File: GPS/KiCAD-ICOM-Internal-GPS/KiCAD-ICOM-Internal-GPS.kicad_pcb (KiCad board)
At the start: 2 copper layers, 2 parts, among them J1 AXK640347YG, U1 MAX-M10M-00B

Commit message: updated schematic & PCB
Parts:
- J1: value AXK640347YG -> ICOM-J1; footprint AXK640347YG:AXK640347YG -> ICOM-J1:ICOM-J1
- moved J1 1.77 mm to (118.3, 59.9)
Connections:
- J1 pad 14: unconnected-(J1-Pad14) -> Net-(J1-RX/OPT1)
- J1 pad 15: unconnected-(J1-Pad15) -> Net-(J1-TX/OPT2)
- J1 pad 17: unconnected-(J1-Pad17) -> Net-(J1-GND-Pad17)
- U1 pad 1: unconnected-(U1-GND-Pad1) -> Net-(J1-GND-Pad17)
- U1 pad 2: unconnected-(U1-TXD-Pad2) -> Net-(J1-RX/OPT1)
- U1 pad 3: unconnected-(U1-RXD-Pad3) -> Net-(J1-TX/OPT2)
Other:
- board outline added: 20 x 35 mm

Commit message: updated schematic a bit
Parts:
- J1: footprint ICOM-J1:ICOM-J1 -> AXK640347YG:AXK640347YG
- moved J1 39.2 mm to (149.4, 83.8)
- moved U1 39.2 mm to (150.3, 96.3)
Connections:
- net Net-(J1-RX/OPT1) renamed GPS-TX
- net Net-(J1-TX/OPT2) renamed GPS-RX
- J1 pad 17: Net-(J1-GND-Pad17) -> GND
- J1 pad 2: unconnected-(J1-GND-Pad2) -> GND
- J1 pad 38: unconnected-(J1-+5V-Pad38) -> +5V
- J1 pad 39: unconnected-(J1-GND-Pad39) -> GND
- U1 pad 1: Net-(J1-GND-Pad17) -> GND
- U1 pad 10: unconnected-(U1-GND-Pad10) -> GND
- U1 pad 11: unconnected-(U1-RF_IN-Pad11) -> ANT-RF
- U1 pad 12: unconnected-(U1-GND-Pad12) -> GND
- U1 pad 13: unconnected-(U1-LNA_EN-Pad13) -> ANT-PWR-ON
- U1 pad 16: unconnected-(U1-SDA-Pad16) -> SDA
- U1 pad 17: unconnected-(U1-SCL-Pad17) -> SCL
- U1 pad 4: unconnected-(U1-TIMEPULSE-Pad4) -> PPS
- U1 pad 5: unconnected-(U1-EXTINT-Pad5) -> EXTINT
- U1 pad 6: unconnected-(U1-V_BCKP-Pad6) -> V-BACKUP
- U1 pad 7: unconnected-(U1-V_IO-Pad7) -> +3.3V
- U1 pad 8: unconnected-(U1-VCC-Pad8) -> +3.3V
- U1 pad 9: unconnected-(U1-RESET_N-Pad9) -> RESET

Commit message: updated v1.0 design
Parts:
- added B1: MS518SE, MS518SE:MS518SE-FL35E, F.Cu at (154.2, 93.2)
- added J2: U.FL-R-SMT-1_10_, U.FL-R-SMT-1_10:HRS_U.FL-R-SMT-1_10_, F.Cu at (143.8, 111.6)
- J1: footprint AXK640347YG:AXK640347YG -> ICOM-J1-J2:ICOM-J1-J2
- moved U1 6.66 mm to (147.1, 102.1), turned to -90 degrees
- moved J1 0.33 mm to (149.3, 83.5)
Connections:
- U1 pad 13: ANT-PWR-ON -> unconnected-(U1-LNA_EN-Pad13)

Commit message: minor save
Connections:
- U1 pad 5: EXTINT -> unconnected-(U1-EXTINT-Pad5)
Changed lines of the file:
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@@
 	(net 44 "V-BACKUP")
 	(net 45 "SCL")
-	(net 46 "EXTINT")
-	(net 47 "SDA")
-	(net 48 "+3.3V")
-	(net 49 "ANT-RF")
-	(net 50 "unconnected-(U1-LNA_EN-Pad13)")
+	(net 46 "SDA")
+	(net 47 "+3.3V")
+	(net 48 "ANT-RF")
+	(net 49 "unconnected-(U1-LNA_EN-Pad13)")
+	(net 50 "unconnected-(U1-EXTINT-Pad5)")
 	(footprint "ICOM-J1-J2:ICOM-J1-J2"
 		(layer "F.Cu")
@@
 		(tags "MAX-M10M-00B ")
 		(property "Reference" "U1"
-			(at 0 0 -90)
+			(at 0 0 0)
 			(unlocked yes)
 			(layer "F.SilkS")
@@
 			(unlocked yes)
 			(layer "F.Fab")
+			(hide yes)
 			(effects
 				(font
@@
 			(layer "F.Fab")
 		)
-		(fp_text user "${REFERENCE}"
-			(at 0 0 -90)
-			(unlocked yes)
-			(layer "F.Fab")
-			(effects
-				(font
-					(size 1 1)
-					(thickness 0.15)
-				)
-			)
-		)
 		(pad "1" smd rect
 			(at -4.4577 -4.399999 270)
@@
 			(size 1.397 0.8382)
 			(layers "F.Cu" "F.Paste" "F.Mask")
-			(net 46 "EXTINT")
+			(net 50 "unconnected-(U1-EXTINT-Pad5)")
 			(pinfunction "EXTINT")
-			(pintype "input")
+			(pintype "input+no_connect")
 		)
 		(pad "6" smd rect
@@
 			(size 1.397 0.8382)
 			(layers "F.Cu" "F.Paste" "F.Mask")
-			(net 48 "+3.3V")
+			(net 47 "+3.3V")
 			(pinfunction "V_IO")
 			(pintype "power_in")
@@
 			(size 1.397 0.8382)
 			(layers "F.Cu" "F.Paste" "F.Mask")
-			(net 48 "+3.3V")
+			(net 47 "+3.3V")
 			(pinfunction "VCC")
 			(pintype "power_in")
@@
 			(size 1.397 0.8382)
 			(layers "F.Cu" "F.Paste" "F.Mask")
-			(net 49 "ANT-RF")
+			(net 48 "ANT-RF")
 			(pinfunction "RF_IN")
 			(pintype "input")
@@
 			(size 1.397 0.8382)
 			(layers "F.Cu" "F.Paste" "F.Mask")
-			(net 50 "unconnected-(U1-LNA_EN-Pad13)")
+			(net 49 "unconnected-(U1-LNA_EN-Pad13)")
 			(pinfunction "LNA_EN")
 			(pintype "output+no_connect")
@@
 			(net 1 "unconnected-(U1-VCC_RF-Pad14)")
 			(pinfunction "VCC_RF")
-			(pintype "output")
+			(pintype "output+no_connect")
 		)
 		(pad "15" smd rect
@@
 			(net 2 "unconnected-(U1-VIO_SEL-Pad15)")
 			(pinfunction "VIO_SEL")
-			(pintype "input")
+			(pintype "input+no_connect")
 		)
 		(pad "16" smd rect
@@
 			(size 1.397 0.8382)
 			(layers "F.Cu" "F.Paste" "F.Mask")
-			(net 47 "SDA")
+			(net 46 "SDA")
 			(pinfunction "SDA")
 			(pintype "bidirectional")
@@
 			(net 3 "unconnected-(U1-SAFEBOOT_N-Pad18)")
 			(pinfunction "SAFEBOOT_N")
-			(pintype "input")
+			(pintype "input+no_connect")
 		)
 		(model "/Users/fredericdruppel/Documents/Documents Importants/Taff/MSF/MSF-Telecom-GitHub/ICOM-Internal-Modules/CAD-Libs/UBX-MAX-M10S/MOD18_MAX-M10M_UBL.step"
@@
 		(at 154.178 93.218 180)
 		(property "Reference" "B1"
-			(at 0 -3.4925 180)
+			(at 0 0 180)
 			(layer "F.SilkS")
 			(effects
@@
 			(at 0 0 180)
 			(layer "F.Fab")
+			(hide yes)
 			(effects
 				(font
@@
 		(at 143.764 111.627 180)
 		(property "Reference" "J2"
-			(at -0.060105 -2.311695 180)
+			(at 0 0 180)
 			(layer "F.SilkS")
 			(effects
@@
 			(at 7.5777 3.09926 180)
 			(layer "F.Fab")
+			(hide yes)
 			(effects
 				(font
@@
 			(size 1 1.05)
 			(layers "F.Cu" "F.Paste" "F.Mask")
-			(net 49 "ANT-RF")
+			(net 48 "ANT-RF")
 			(pintype "passive")
 			(solder_mask_margin 0.102)

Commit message: updated schematic and pcb
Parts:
- added C1: 10nF, Capacitor_SMD:C_0603_1608Metric, F.Cu at (144.5, 108.7)
- added C2: 10nF, Capacitor_SMD:C_0603_1608Metric, F.Cu at (143.5, 95.8)
- added C3: 10nF, Capacitor_SMD:C_0603_1608Metric, F.Cu at (146.8, 95.8)
- added C4: 10nF, Capacitor_SMD:C_0603_1608Metric, F.Cu at (140.0, 91.4)
- added J3: Conn_01x08, Connector_PinSocket_2.54mm:PinSocket_1x08_P2.54mm_Vertical, F.Cu at (156.2, 93.7)
- added L1: 27nH, Inductor_SMD:L_0402_1005Metric, F.Cu at (143.0, 111.5)
- added R1: 10, Resistor_SMD:R_0603_1608Metric, F.Cu at (144.5, 110.2)
- added U2: TC2015-3.3VxCTTR, Package_TO_SOT_SMD:SOT-23-5, F.Cu at (142.5, 91.4)
- moved J2 4.19 mm to (139.6, 111.5), turned to 90 degrees
- moved B1 3.28 mm to (150.9, 93.2)
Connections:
- J2 pad 2: ANT-RF -> Net-(J2-Pad2)

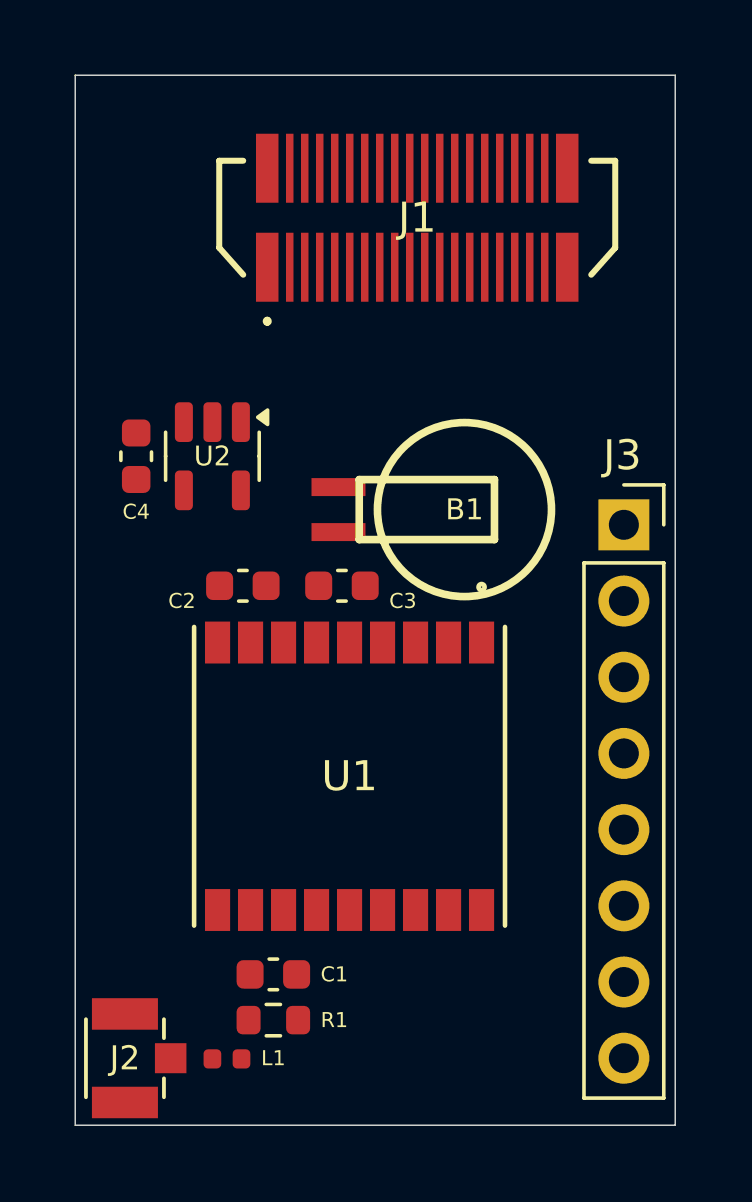
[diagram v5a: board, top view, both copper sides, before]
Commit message: Routed traces
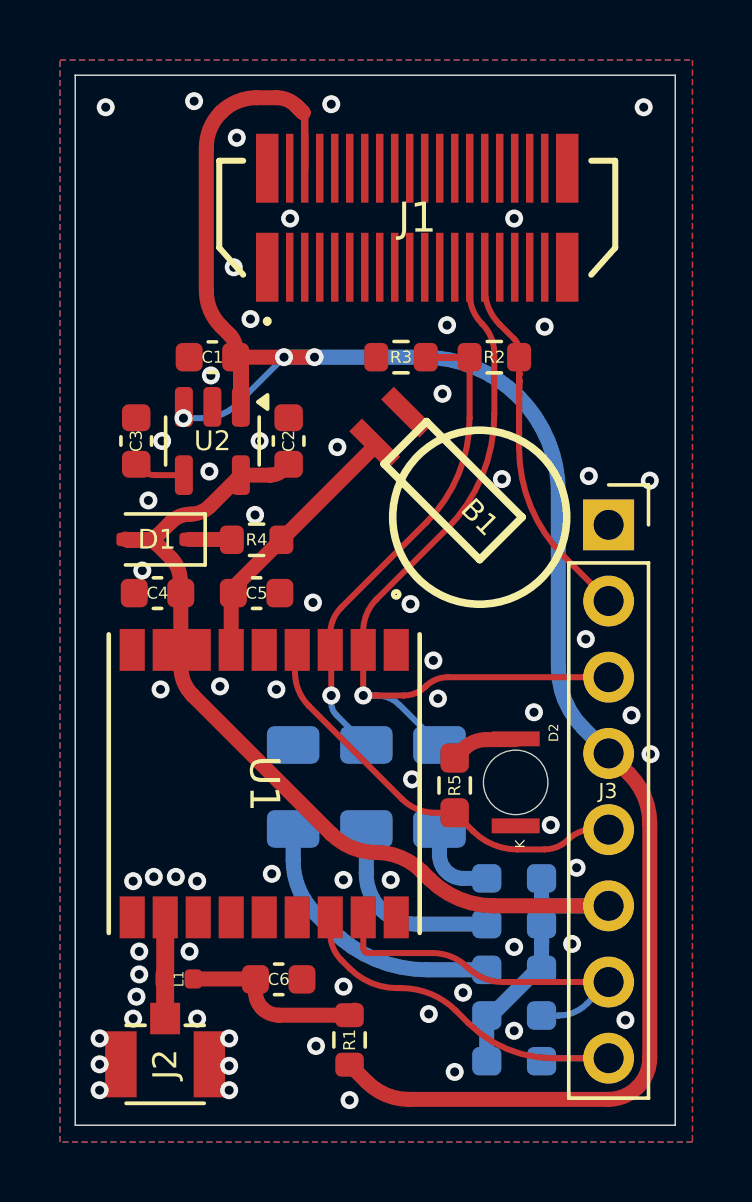
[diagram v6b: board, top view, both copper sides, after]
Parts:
- added C5: 10nF, Capacitor_SMD:C_0603_1608Metric, F.Cu at (144.0, 96.0)
- added C6: 10nF, Capacitor_SMD:C_0603_1608Metric, F.Cu at (144.7, 108.9)
- added D1: D_Schottky, Diode_SMD:D_SOD-323, F.Cu at (140.6, 94.2)
- added D2: KPTR-3216SURCK, KINGBRIGHT KPTR-3216SURCK:LED320X125X130N, F.Cu at (152.6, 102.3)
- added D3: LED, LED_SMD:LED_1206_3216Metric, B.Cu at (145.2, 102.5)
- added D4: LED, LED_SMD:LED_1206_3216Metric, B.Cu at (147.6, 102.5)
- added D5: LED, LED_SMD:LED_1206_3216Metric, B.Cu at (150.1, 102.5)
- added R10: 3.3k, Resistor_SMD:R_0603_1608Metric_Pad0.98x0.95mm_HandSolder, B.Cu at (152.6, 111.6)
- added R2: 3.3k, Resistor_SMD:R_0603_1608Metric, F.Cu at (151.9, 88.1)
- added R3: 3.3k, Resistor_SMD:R_0603_1608Metric, F.Cu at (148.8, 88.1)
- added R4: 3.3k, Resistor_SMD:R_0603_1608Metric, F.Cu at (144.0, 94.2)
- added R5: 220, Resistor_SMD:R_0603_1608Metric_Pad0.98x0.95mm_HandSolder, F.Cu at (150.6, 102.4)
- added R6: 220, Resistor_SMD:R_0603_1608Metric_Pad0.98x0.95mm_HandSolder, B.Cu at (152.6, 108.6)
- added R7: 220, Resistor_SMD:R_0603_1608Metric_Pad0.98x0.95mm_HandSolder, B.Cu at (152.6, 107.0)
- added R8: 220, Resistor_SMD:R_0603_1608Metric_Pad0.98x0.95mm_HandSolder, B.Cu at (152.6, 105.5)
- added R9: 3.3k, Resistor_SMD:R_0603_1608Metric_Pad0.98x0.95mm_HandSolder, B.Cu at (152.6, 110.1)
- C1, C2: value 10nF -> 1uF
- moved C1 20.7 mm to (142.5, 88.1), turned to 180 degrees
- moved C3 8.39 mm to (140.0, 90.9), turned to 90 degrees
- moved C2 5.06 mm to (145.0, 90.9), turned to 90 degrees
- moved C4 4.62 mm to (140.7, 96.0), turned to 180 degrees
- moved L1 3.11 mm to (141.4, 108.9)
- moved U1 2.86 mm to (144.2, 102.4)
- moved R1 2.62 mm to (147.1, 110.9), turned to 90 degrees
- moved J2 1.36 mm to (140.9, 111.7), turned to 180 degrees
- moved B1 0.57 mm to (151.4, 93.5), turned to 135 degrees
- moved J3 0.51 mm to (155.7, 93.7)
- moved U2 0.51 mm to (142.5, 90.9)
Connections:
- C1 pad 1: ANT-RF -> +5V
- C3 pad 1: V-BACKUP -> Net-(U2-BP)
- C4 pad 1: Net-(U2-BP) -> +3.3V
- J1 pad 15: GPS-RX -> GPS-RX-Protected
- J2 pad 2: Net-(J2-Pad2) -> ANT-RF
- J3 pad 2: GPS-TX -> GPS-RX-Protected
- J3 pad 3: GPS-RX -> GPS-TX
- J3 pad 4: +3.3V -> +5V
- J3 pad 5: +5V -> PPS
- J3 pad 6: PPS -> +3.3V
- J3 pad 7: SDA -> SCL
- J3 pad 8: SCL -> SDA
- L1 pad 1: ANT-RF -> Net-(C6-Pad1)
- L1 pad 2: Net-(J2-Pad2) -> ANT-RF
- R1 pad 2: ANT-RF -> Net-(C6-Pad1)
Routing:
- net +5V: track 0.00 -> 66.1 mm, vias 0 -> 3
- net +3.3V: track 0.00 -> 40.7 mm
- net GPS-TX: track 0.00 -> 28.0 mm, vias 0 -> 1
- net GPS-RX: track 0.00 -> 16.4 mm, vias 0 -> 1
- net PPS: track 0.00 -> 14.7 mm
- net SDA: track 0.00 -> 14.2 mm
- net GPS-RX-Protected: track 0.00 -> 13.3 mm
- net SCL: track 0.00 -> 12.3 mm
- net Net-(D3-A): track 0.00 -> 9.28 mm
- net V-BACKUP: track 0.00 -> 8.82 mm
- net Net-(C6-Pad1): track 0.00 -> 6.54 mm
- net Net-(D4-A): track 0.00 -> 3.78 mm
- net ANT-RF: track 0.00 -> 3.42 mm
- net Net-(D5-A): track 0.00 -> 2.85 mm
- net Net-(D2-A): track 0.00 -> 2.24 mm
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- added copper zone on B.Cu, net GND
- added copper zone on F.Cu, net GND

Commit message: saved changes from KiCAD
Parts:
- added F1: Fiducial_0.5mm_Mask1.5mm, Fiducial:Fiducial_0.5mm_Mask1.5mm, F.Cu at (140.0, 82.7)
- added F2: Fiducial_0.5mm_Mask1.5mm, Fiducial:Fiducial_0.5mm_Mask1.5mm, F.Cu at (155.7, 90.5)
- D1: value D_Schottky -> RB551V-40
- D3: value LED -> XL-3216SURC
- D4, D5: value LED -> XL-3216UOC
- U2: value TC2015-3.3VxCTTR -> SPX5205
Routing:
- net GND: vias 66 -> 67
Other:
- board text added: "Baudrate : 4800 9600"
- board text added: "MSF - 03-2024 Frédéric Druppel"
- board text added: "PPS"
- board text added: "PWR"
- board text added: "RX"
- board text added: "Serial n°"
- board text added: "TX"
- board text added: "UT-GPS v1.0"
